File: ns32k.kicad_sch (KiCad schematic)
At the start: 50 parts, among them SW2 SW_DIP_x04, U1 NS32201, U10 74AHC373, U11 74AHC373, U12 74AHC138, U13 AS6C6416-55, U15 MX29LV040C, U16 MX29LV040C, U19 74AHC138, U20 74AHC1G08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

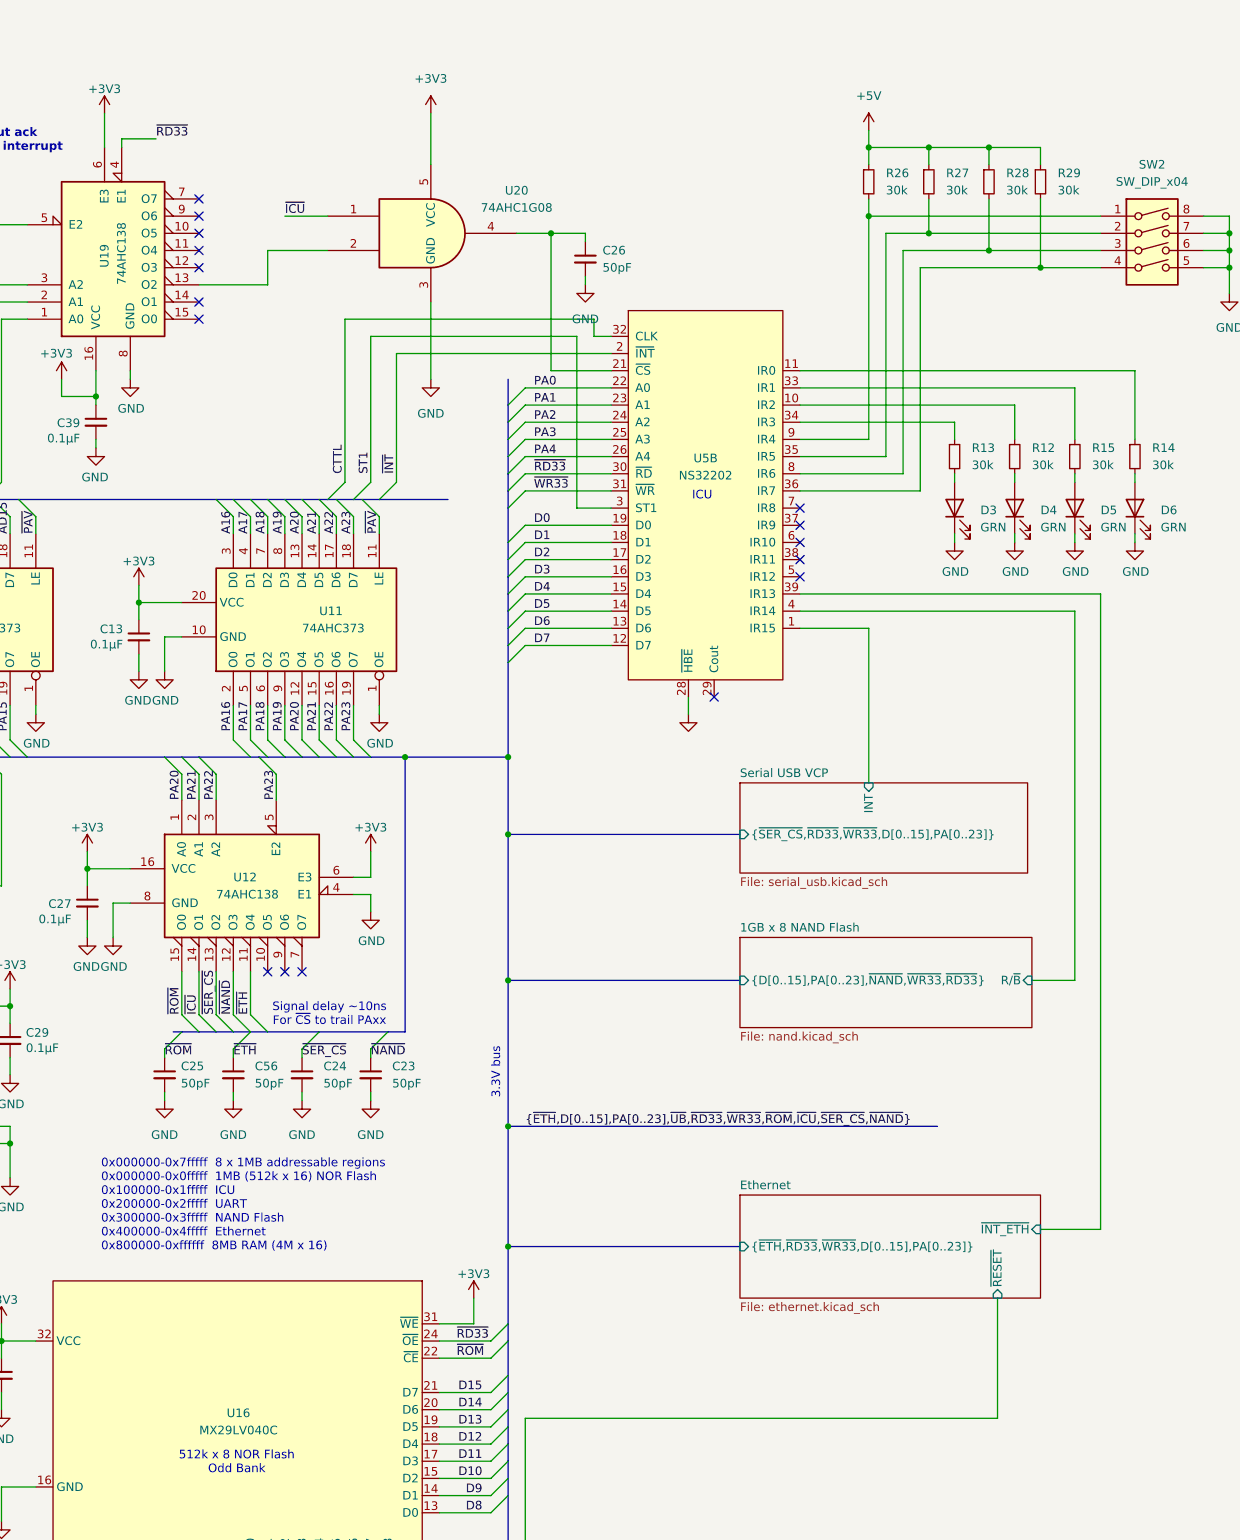
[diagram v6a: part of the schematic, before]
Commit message: route ethernet, reroute USB
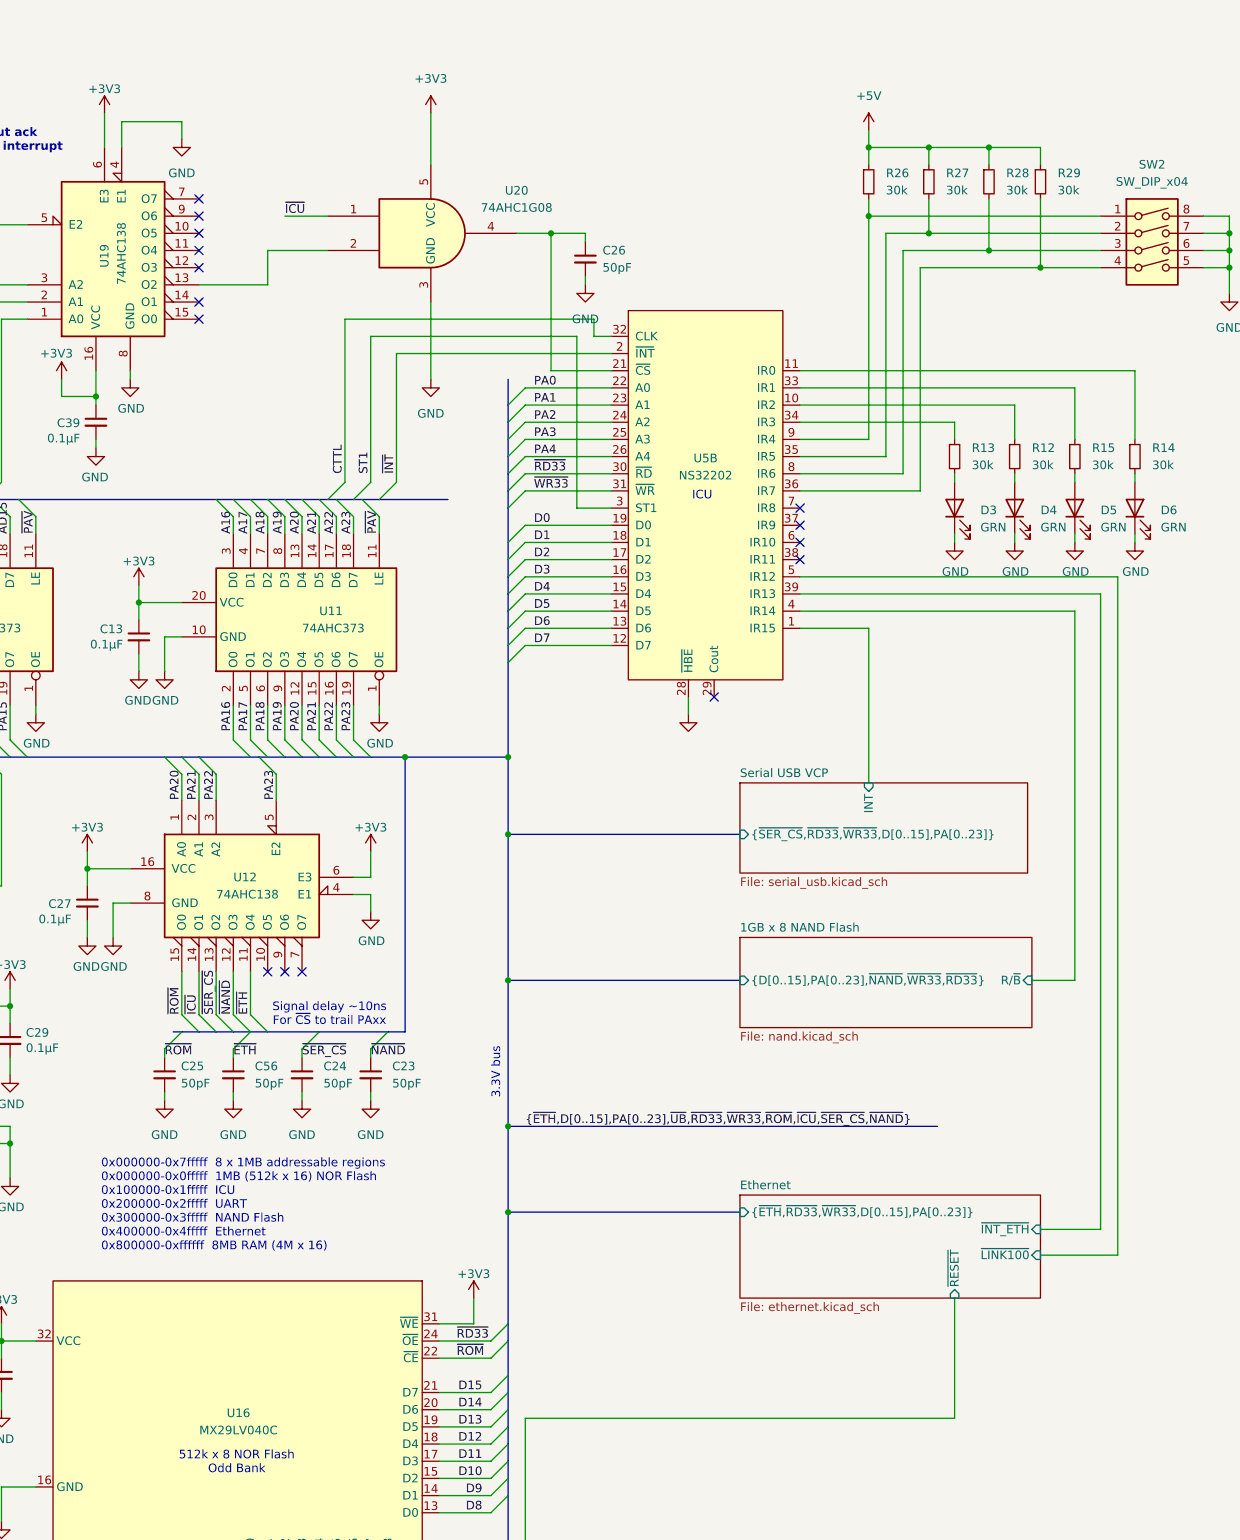
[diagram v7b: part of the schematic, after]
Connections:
- net GND: now also U19.4 (E1)
- net ~{RD33}: no longer U19.4 (E1)
- net Ethernet/~{LINK100}: now reaches U5.5 (IR12)
- no-connect marks 19 -> 18
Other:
- sheet Ethernet ports: added ~{LINK100}; removed none
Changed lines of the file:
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@@
 	)
 	(junction
+		(at 293.37 181.61)
+		(diameter 0)
+		(color 0 0 0 0)
+	)
+	(junction
 		(at 92.71 238.76)
 		(diameter 0)
@@
 	)
 	(junction
-		(at 293.37 186.69)
-		(diameter 0)
-		(color 0 0 0 0)
-	)
-	(junction
 		(at 30.48 237.49)
 		(diameter 0)
@@
 	)
 	(no_connect
-		(at 336.55 87.63)
-	)
-	(no_connect
 		(at 336.55 82.55)
 	)
@@
 	(wire
 		(pts
-			(xy 365.76 212.09) (xy 365.76 194.31)
+			(xy 359.41 212.09) (xy 359.41 194.31)
 		)
 		(stroke
@@
 	(wire
 		(pts
-			(xy 295.91 212.09) (xy 365.76 212.09)
+			(xy 295.91 212.09) (xy 359.41 212.09)
 		)
 		(stroke
@@
 	(bus
 		(pts
-			(xy 293.37 186.69) (xy 327.66 186.69)
+			(xy 293.37 181.61) (xy 327.66 181.61)
 		)
 		(stroke
@@
 	(bus
 		(pts
-			(xy 293.37 168.91) (xy 293.37 186.69)
+			(xy 293.37 168.91) (xy 293.37 181.61)
 		)
 		(stroke
@@
 	(wire
 		(pts
-			(xy 236.22 22.86) (xy 236.22 24.13)
+			(xy 236.22 20.32) (xy 236.22 24.13)
 		)
 		(stroke
@@
 	(wire
 		(pts
+			(xy 383.54 187.96) (xy 383.54 87.63)
+		)
+		(stroke
+			(width 0)
+			(type default)
+		)
+	)
+	(wire
+		(pts
 			(xy 377.19 92.71) (xy 336.55 92.71)
 		)
@@
 	(wire
 		(pts
+			(xy 245.11 22.86) (xy 245.11 20.32)
+		)
+		(stroke
+			(width 0)
+			(type default)
+		)
+	)
+	(wire
+		(pts
 			(xy 396.24 39.37) (xy 400.05 39.37)
 		)
@@
 		)
 	)
-	(bus
-		(pts
-			(xy 293.37 186.69) (xy 293.37 198.12)
-		)
-		(stroke
-			(width 0)
-			(type default)
-		)
-	)
 	(wire
 		(pts
@@
 		)
 	)
+	(wire
+		(pts
+			(xy 372.11 187.96) (xy 383.54 187.96)
+		)
+		(stroke
+			(width 0)
+			(type default)
+		)
+	)
 	(bus
 		(pts
@@
 	(bus
 		(pts
+			(xy 293.37 181.61) (xy 293.37 198.12)
+		)
+		(stroke
+			(width 0)
+			(type default)
+		)
+	)
+	(bus
+		(pts
 			(xy 293.37 67.31) (xy 293.37 69.85)
 		)
@@
 	(wire
 		(pts
+			(xy 383.54 87.63) (xy 336.55 87.63)
+		)
+		(stroke
+			(width 0)
+			(type default)
+		)
+	)
+	(wire
+		(pts
 			(xy 85.09 133.35) (xy 91.44 133.35)
 		)
@@
 	(wire
 		(pts
-			(xy 236.22 22.86) (xy 241.3 22.86)
+			(xy 236.22 20.32) (xy 245.11 20.32)
 		)
 		(stroke
@@
 		)
 	)
-	(label "~{RD33}"
-		(at 241.3 22.86 0)
-		(fields_autoplaced yes)
-		(effects
-			(font
-				(size 1.27 1.27)
-			)
-			(justify left bottom)
-		)
-	)
 	(label "~{INT}"
 		(at 62.23 67.31 90)
@@
 	(symbol
 		(lib_id "power:GND")
+		(at 245.11 22.86 0)
+		(unit 1)
+		(exclude_from_sim no)
+		(in_bom yes)
+		(on_board yes)
+		(dnp no)
+		(fields_autoplaced yes)
+		(property "Reference" "#PWR0144"
+			(at 245.11 29.21 0)
+			(effects
+				(font
+					(size 1.27 1.27)
+				)
+				(hide yes)
+			)
+		)
+		(property "Value" "GND"
+			(at 245.11 27.94 0)
+			(effects
+				(font
+					(size 1.27 1.27)
+				)
+			)
+		)
+		(property "Footprint" ""
+			(at 245.11 22.86 0)
+			(effects
+				(font
+					(size 1.27 1.27)
+				)
+				(hide yes)
+			)
+		)
+		(property "Datasheet" ""
+			(at 245.11 22.86 0)
+			(effects
+				(font
+					(size 1.27 1.27)
+				)
+				(hide yes)
+			)
+		)
+		(property "Description" "Power symbol creates a global label with name \"GND\" , ground"
+			(at 245.11 22.86 0)
+			(effects
+				(font
+					(size 1.27 1.27)
+				)
+				(hide yes)
+			)
+		)
+		(pin "1"
+		)
+		(instances
+			(project ""
+				(path "/54787df0-1b8c-465f-acae-f55ec7f02da3"
+					(reference "#PWR0144")
+					(unit 1)
+				)
+			)
+		)
+	)
+	(symbol
+		(lib_id "power:GND")
 		(at 368.3 82.55 0)
 		(unit 1)
@@
 		)
 		(pin "{~{ETH},~{RD33},~{WR33},D[0..15],PA[0..23]}" input
-			(at 327.66 186.69 180)
+			(at 327.66 181.61 180)
 			(effects
 				(font
@@
 		)
 		(pin "~{RESET}" input
-			(at 365.76 194.31 270)
+			(at 359.41 194.31 270)
 			(effects
 				(font
@@
 			)
 		)
+		(pin "~{LINK100}" input
+			(at 372.11 187.96 0)
+			(effects
+				(font
+					(size 1.27 1.27)
+				)
+				(justify right)
+			)
+		)

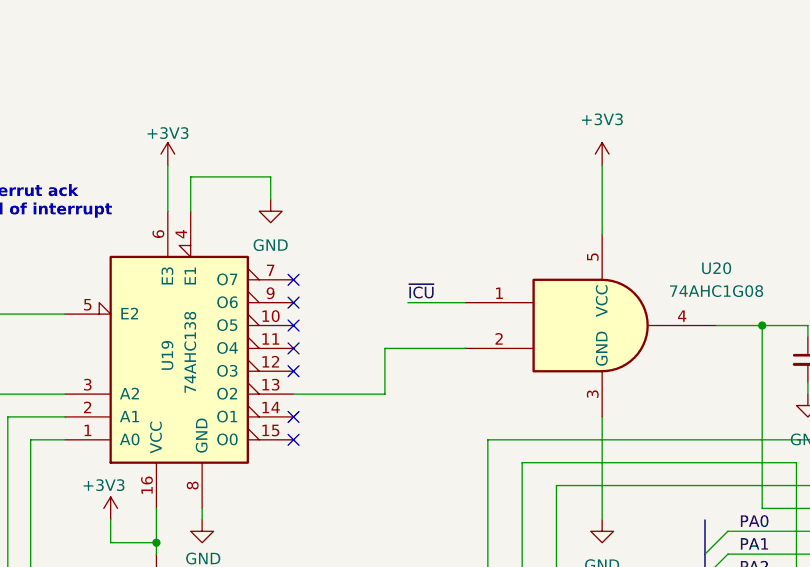
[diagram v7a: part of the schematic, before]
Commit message: add 0R's to ICU CS logic
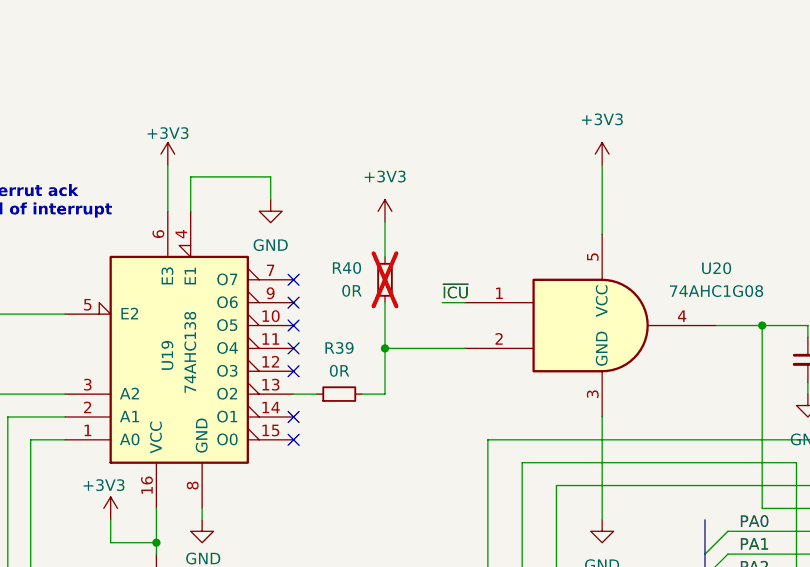
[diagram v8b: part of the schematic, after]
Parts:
- added R39, R40: 0R, Resistor_SMD:R_0402_1005Metric, symbol Device:R_Small
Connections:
- net +3V3: now also R40.2
- net at U20.2: now also R39.2, R40.1; no longer U19.13 (O2)
- new net: R39.1, U19.13 (O2)
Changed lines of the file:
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@@
 		(color 0 0 0 0)
 	)
+	(junction
+		(at 257.81 39.37)
+		(diameter 0)
+		(color 0 0 0 0)
+	)
 	(no_connect
 		(at 247.65 41.91)
@@
 	(wire
 		(pts
-			(xy 257.81 44.45) (xy 247.65 44.45)
+			(xy 257.81 44.45) (xy 255.27 44.45)
 		)
 		(stroke
@@
 	(wire
 		(pts
-			(xy 260.35 34.29) (xy 266.7 34.29)
+			(xy 264.16 34.29) (xy 266.7 34.29)
 		)
 		(stroke
@@
 		)
 	)
+	(wire
+		(pts
+			(xy 257.81 34.29) (xy 257.81 39.37)
+		)
+		(stroke
+			(width 0)
+			(type default)
+		)
+	)
 	(bus
 		(pts
@@
 	(wire
 		(pts
+			(xy 257.81 25.4) (xy 257.81 29.21)
+		)
+		(stroke
+			(width 0)
+			(type default)
+		)
+	)
+	(wire
+		(pts
 			(xy 80.01 204.47) (xy 80.01 205.74)
 		)
@@
 	(wire
 		(pts
+			(xy 250.19 44.45) (xy 247.65 44.45)
+		)
+		(stroke
+			(width 0)
+			(type default)
+		)
+	)
+	(wire
+		(pts
 			(xy 223.52 222.25) (xy 218.44 222.25)
 		)
@@
 	)
 	(label "~{ICU}"
-		(at 260.35 34.29 0)
+		(at 264.16 34.29 0)
 		(fields_autoplaced yes)
 		(effects
@@
 	)
 	(symbol
+		(lib_id "power:+3V3")
+		(at 257.81 25.4 0)
+		(unit 1)
+		(exclude_from_sim no)
+		(in_bom yes)
+		(on_board yes)
+		(dnp no)
+		(fields_autoplaced yes)
+		(property "Reference" "#PWR0149"
+			(at 257.81 29.21 0)
+			(effects
+				(font
+					(size 1.27 1.27)
+				)
+				(hide yes)
+			)
+		)
+		(property "Value" "+3V3"
+			(at 257.81 20.32 0)
+			(effects
+				(font
+					(size 1.27 1.27)
+				)
+			)
+		)
+		(property "Footprint" ""
+			(at 257.81 25.4 0)
+			(effects
+				(font
+					(size 1.27 1.27)
+				)
+				(hide yes)
+			)
+		)
+		(property "Datasheet" ""
+			(at 257.81 25.4 0)
+			(effects
+				(font
+					(size 1.27 1.27)
+				)
+				(hide yes)
+			)
+		)
+		(property "Description" "Power symbol creates a global label with name \"+3V3\""
+			(at 257.81 25.4 0)
+			(effects
+				(font
+					(size 1.27 1.27)
+				)
+				(hide yes)
+			)
+		)
+		(pin "1"
+		)
+		(instances
+			(project ""
+				(path "/54787df0-1b8c-465f-acae-f55ec7f02da3"
+					(reference "#PWR0149")
+					(unit 1)
+				)
+			)
+		)
+	)
+	(symbol
 		(lib_id "power:GND")
 		(at 377.19 82.55 0)
@@
 	)
 	(symbol
+		(lib_id "Device:R_Small")
+		(at 257.81 31.75 0)
+		(mirror x)
+		(unit 1)
+		(exclude_from_sim no)
+		(in_bom yes)
+		(on_board yes)
+		(dnp yes)
+		(property "Reference" "R40"
+			(at 255.27 30.4799 0)
+			(effects
+				(font
+					(size 1.27 1.27)
+				)
+				(justify right)
+			)
+		)
+		(property "Value" "0R"
+			(at 255.27 33.0199 0)
+			(effects
+				(font
+					(size 1.27 1.27)
+				)
+				(justify right)
+			)
+		)
+		(property "Footprint" "Resistor_SMD:R_0402_1005Metric"
+			(at 257.81 31.75 0)
+			(effects
+				(font
+					(size 1.27 1.27)
+				)
+				(hide yes)
+			)
+		)
+		(property "Datasheet" "~"
+			(at 257.81 31.75 0)
+			(effects
+				(font
+					(size 1.27 1.27)
+				)
+				(hide yes)
+			)
+		)
+		(property "Description" "Resistor, small symbol"
+			(at 257.81 31.75 0)
+			(effects
+				(font
+					(size 1.27 1.27)
+				)
+				(hide yes)
+			)
+		)
+		(pin "1"
+		)
+		(pin "2"
+		)
+		(instances
+			(project "ns32k"
+				(path "/54787df0-1b8c-465f-acae-f55ec7f02da3"
+					(reference "R40")
+					(unit 1)
+				)
+			)
+		)
+	)
+	(symbol
 		(lib_id "power:GND")
 		(at 232.41 68.58 0)
@@
 					(unit 1)
 				)
+			)
+		)
+	)
+	(symbol
+		(lib_id "Device:R_Small")
+		(at 252.73 44.45 90)
+		(unit 1)
+		(exclude_from_sim no)
+		(in_bom yes)
+		(on_board yes)
+		(dnp no)
+		(fields_autoplaced yes)
+		(property "Reference" "R39"
+			(at 252.73 39.37 90)
+			(effects
+				(font
+					(size 1.27 1.27)
+				)
+			)
+		)
+		(property "Value" "0R"
+			(at 252.73 41.91 90)
+			(effects
+				(font
+					(size 1.27 1.27)
+				)
+			)
+		)
+		(property "Footprint" "Resistor_SMD:R_0402_1005Metric"
+			(at 252.73 44.45 0)
+			(effects
+				(font
+					(size 1.27 1.27)
+				)
+				(hide yes)
+			)
+		)
+		(property "Datasheet" "~"
+			(at 252.73 44.45 0)
+			(effects
+				(font
+					(size 1.27 1.27)
+				)
+				(hide yes)
+			)
+		)
+		(property "Description" "Resistor, small symbol"
+			(at 252.73 44.45 0)
+			(effects
+				(font
+					(size 1.27 1.27)
+				)
+				(hide yes)
+			)
+		)
+		(pin "1"
+		)
+		(pin "2"
+		)
+		(instances
+			(project "ns32k"
+				(path "/54787df0-1b8c-465f-acae-f55ec7f02da3"
+					(reference "R39")
+					(unit 1)
+				)
